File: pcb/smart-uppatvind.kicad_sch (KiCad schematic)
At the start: 65 parts, among them J1 PWR, J2 QWIIC, J3 UART_PROG, J4 FAN, Q1 IRLML9301, Q2 MMBT3904, Q3 MMBT3904, Q4 MMBT3904, Q5 Q_NMOS_GSD, SW1 EN, SW2 MAIN, SW3 BOOT, SW4 FILTER, U1 LDL1117S33R, U2 L7980A, U3 ESP32-C3-WROOM-02, U4 M24C02-WMN

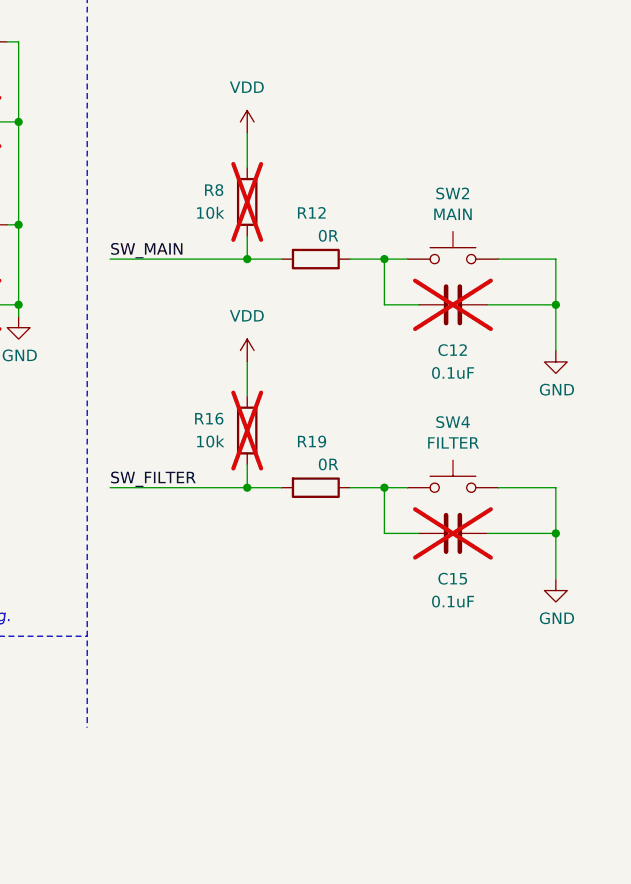
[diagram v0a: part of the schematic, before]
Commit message: Connected shield pins of filter switch, made switch pull-ups not optional
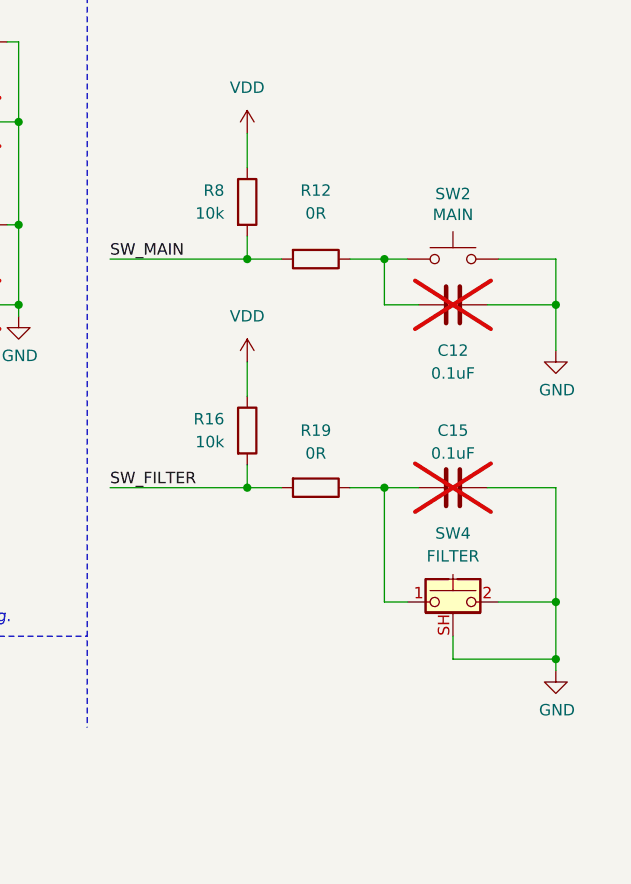
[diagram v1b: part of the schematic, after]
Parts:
- removed SW4: FILTER, Moucha_Primitives:SW_Tactile_G-Switch_GT-TC102B_Angled, symbol Switch:SW_Push
- added SW4: FILTER, Moucha_Primitives:SW_Tactile_G-Switch_GT-TC102B_Angled, symbol Switch:SW_Push_Shielded
- R16, R8: now fitted
- SW2: LCSC C589212 -> (none)
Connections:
- net GND: now also SW4.2, SW4.SH (B)
- net at C15.2, R19.1: now also SW4.1
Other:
- moved on the sheet: C15

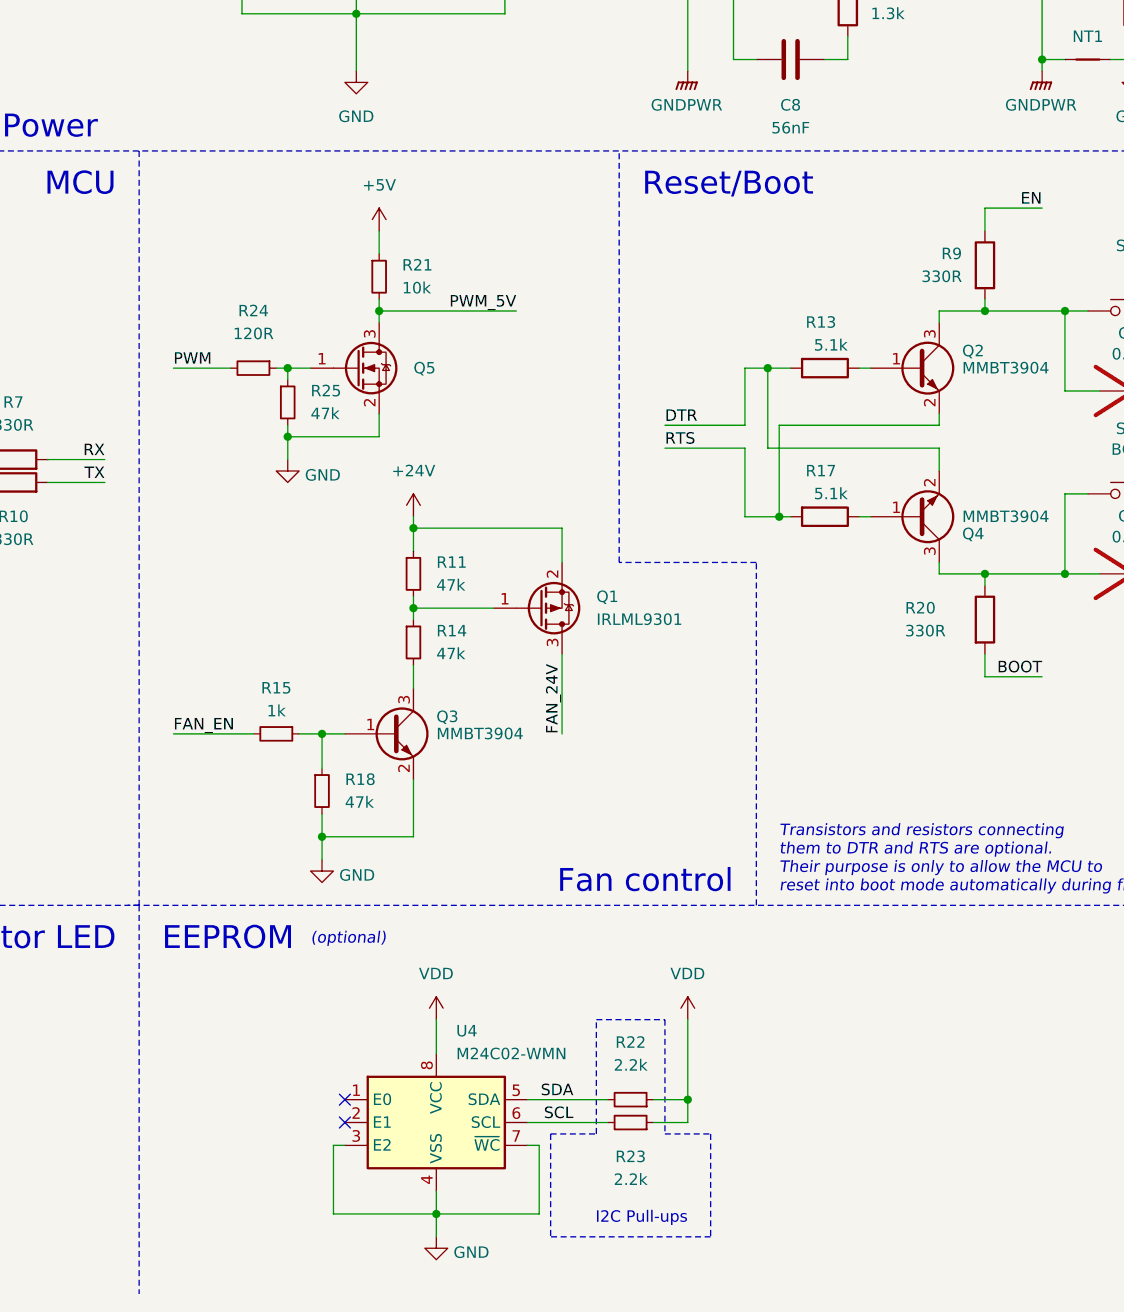
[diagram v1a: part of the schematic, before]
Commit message: Removed R_Small symbols for consistency
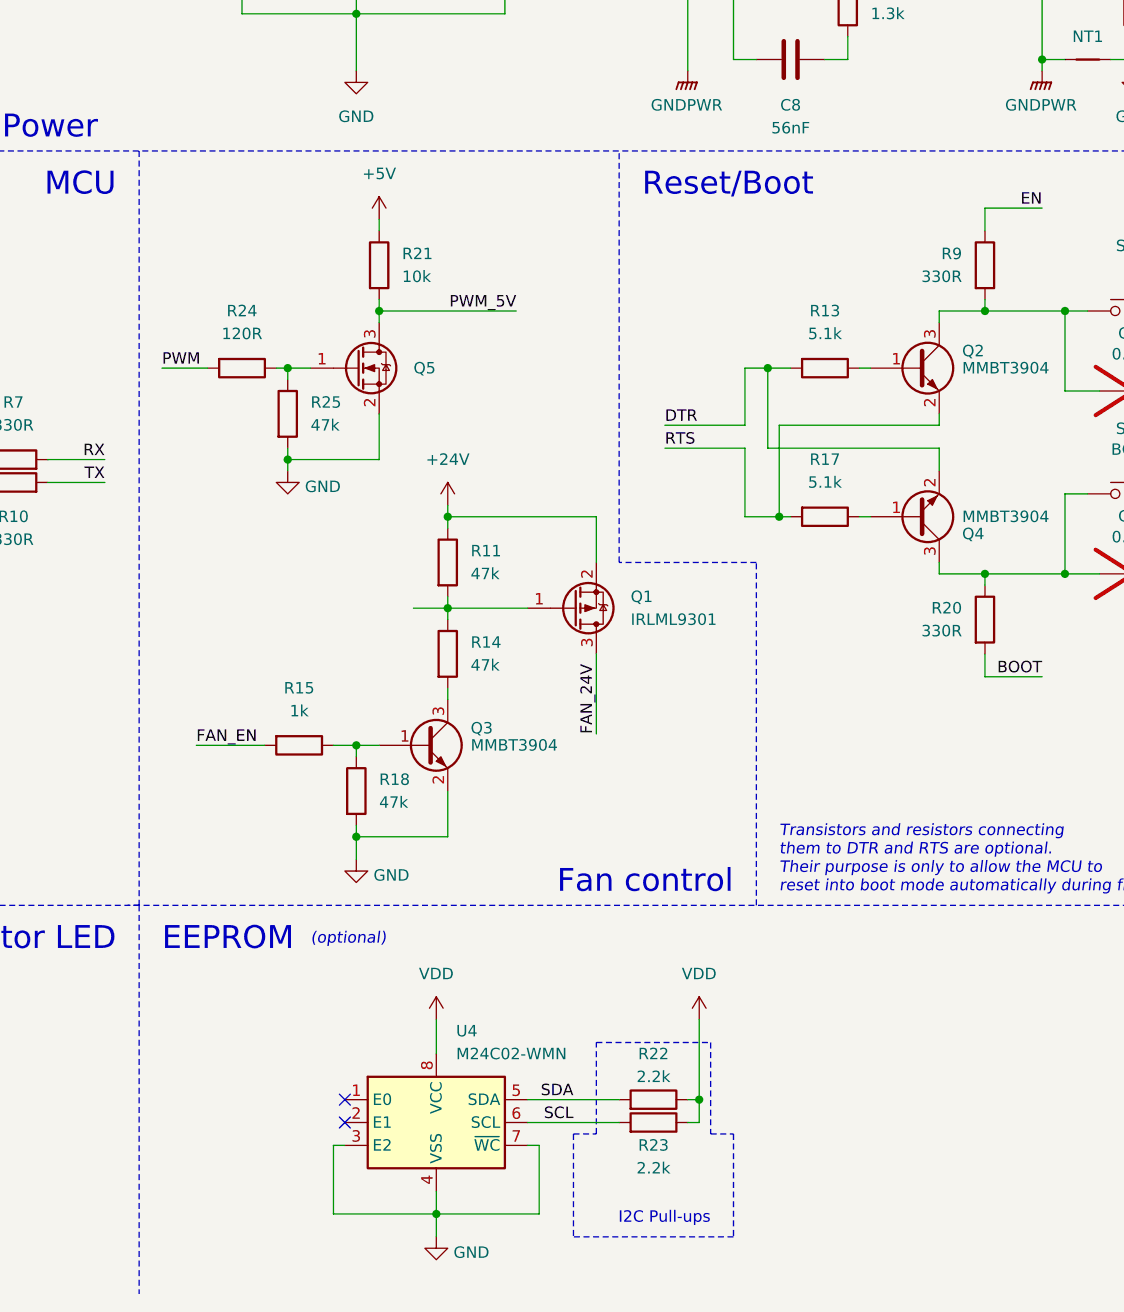
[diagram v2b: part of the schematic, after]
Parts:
- C12, C13, C14, C15: now in the parts list
- R11, R14, R15, R18, R21, R22, R23, R24, R25: symbol Device:R_Small -> Device:R
- R12, R13, R17, R19: LCSC C25905 -> (none)
- R16, R20, R8, R9: LCSC C25104 -> (none)
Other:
- moved on the sheet: Q1, Q3, R11, R14, R15, R18, R21, R22, R23, R24, R25

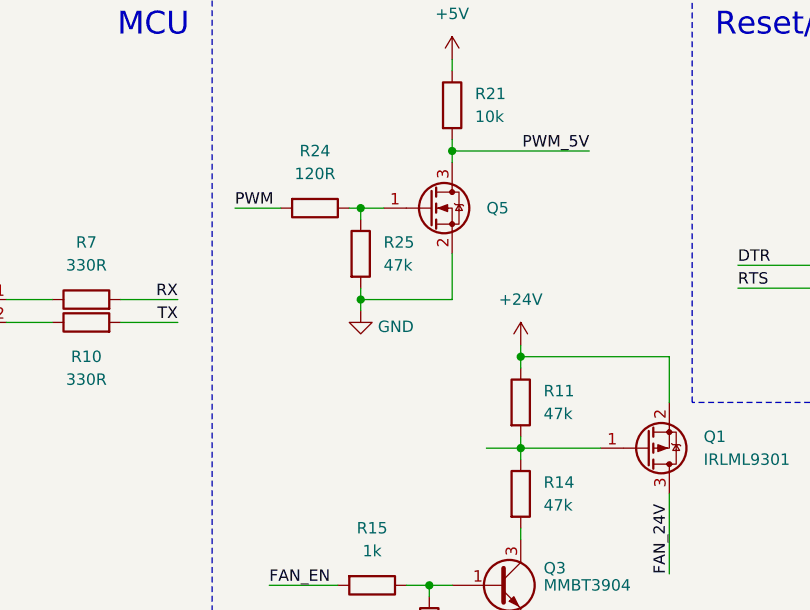
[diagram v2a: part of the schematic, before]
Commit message: Unified resistor footprints - removed handsolder variants
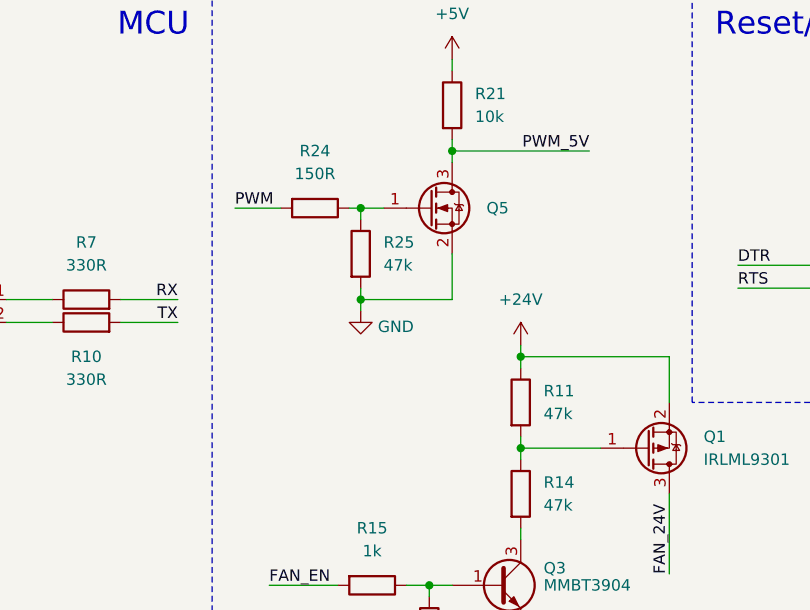
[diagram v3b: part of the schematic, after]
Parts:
- R11, R14, R15, R18, R21, R25: footprint Resistor_SMD:R_0805_2012Metric_Pad1.20x1.40mm_HandSolder -> Resistor_SMD:R_0805_2012Metric
- R24: value 120R -> 150R; footprint Resistor_SMD:R_0805_2012Metric_Pad1.20x1.40mm_HandSolder -> Resistor_SMD:R_0805_2012Metric
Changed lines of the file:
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@@
 	(wire
 		(pts
-			(xy 135.89 121.92) (xy 132.08 121.92)
-		)
-		(stroke
-			(width 0)
-			(type default)
-		)
-	)
-	(wire
-		(pts
 			(xy 154.94 35.56) (xy 167.64 35.56)
 		)
@@
 			)
 		)
-		(property "Footprint" "Resistor_SMD:R_0805_2012Metric_Pad1.20x1.40mm_HandSolder"
+		(property "Footprint" "Resistor_SMD:R_0805_2012Metric"
 			(at 128.27 83.82 0)
 			(effects
@@
 			)
 		)
-		(property "Footprint" "Resistor_SMD:R_0805_2012Metric_Pad1.20x1.40mm_HandSolder"
+		(property "Footprint" "Resistor_SMD:R_0805_2012Metric"
 			(at 134.112 127 90)
 			(effects
@@
 			)
 		)
-		(property "Footprint" "Resistor_SMD:R_0805_2012Metric_Pad1.20x1.40mm_HandSolder"
+		(property "Footprint" "Resistor_SMD:R_0805_2012Metric"
 			(at 119.38 135.382 90)
 			(effects
@@
 			)
 		)
-		(property "Footprint" "Resistor_SMD:R_0805_2012Metric_Pad1.20x1.40mm_HandSolder"
+		(property "Footprint" "Resistor_SMD:R_0805_2012Metric"
 			(at 118.11 100.33 0)
 			(effects
@@
 			)
 		)
-		(property "Footprint" "Resistor_SMD:R_0805_2012Metric_Pad1.20x1.40mm_HandSolder"
+		(property "Footprint" "Resistor_SMD:R_0805_2012Metric"
 			(at 134.112 116.84 90)
 			(effects
@@
 			)
 		)
-		(property "Value" "120R"
+		(property "Value" "150R"
 			(at 113.03 91.44 90)
 			(effects
@@
 			)
 		)
-		(property "Footprint" "Resistor_SMD:R_0805_2012Metric_Pad1.20x1.40mm_HandSolder"
+		(property "Footprint" "Resistor_SMD:R_0805_2012Metric"
 			(at 113.03 95.25 0)
 			(effects
@@
 			)
 		)
-		(property "Footprint" "Resistor_SMD:R_0805_2012Metric_Pad1.20x1.40mm_HandSolder"
+		(property "Footprint" "Resistor_SMD:R_0805_2012Metric"
 			(at 123.952 142.24 90)
 			(effects

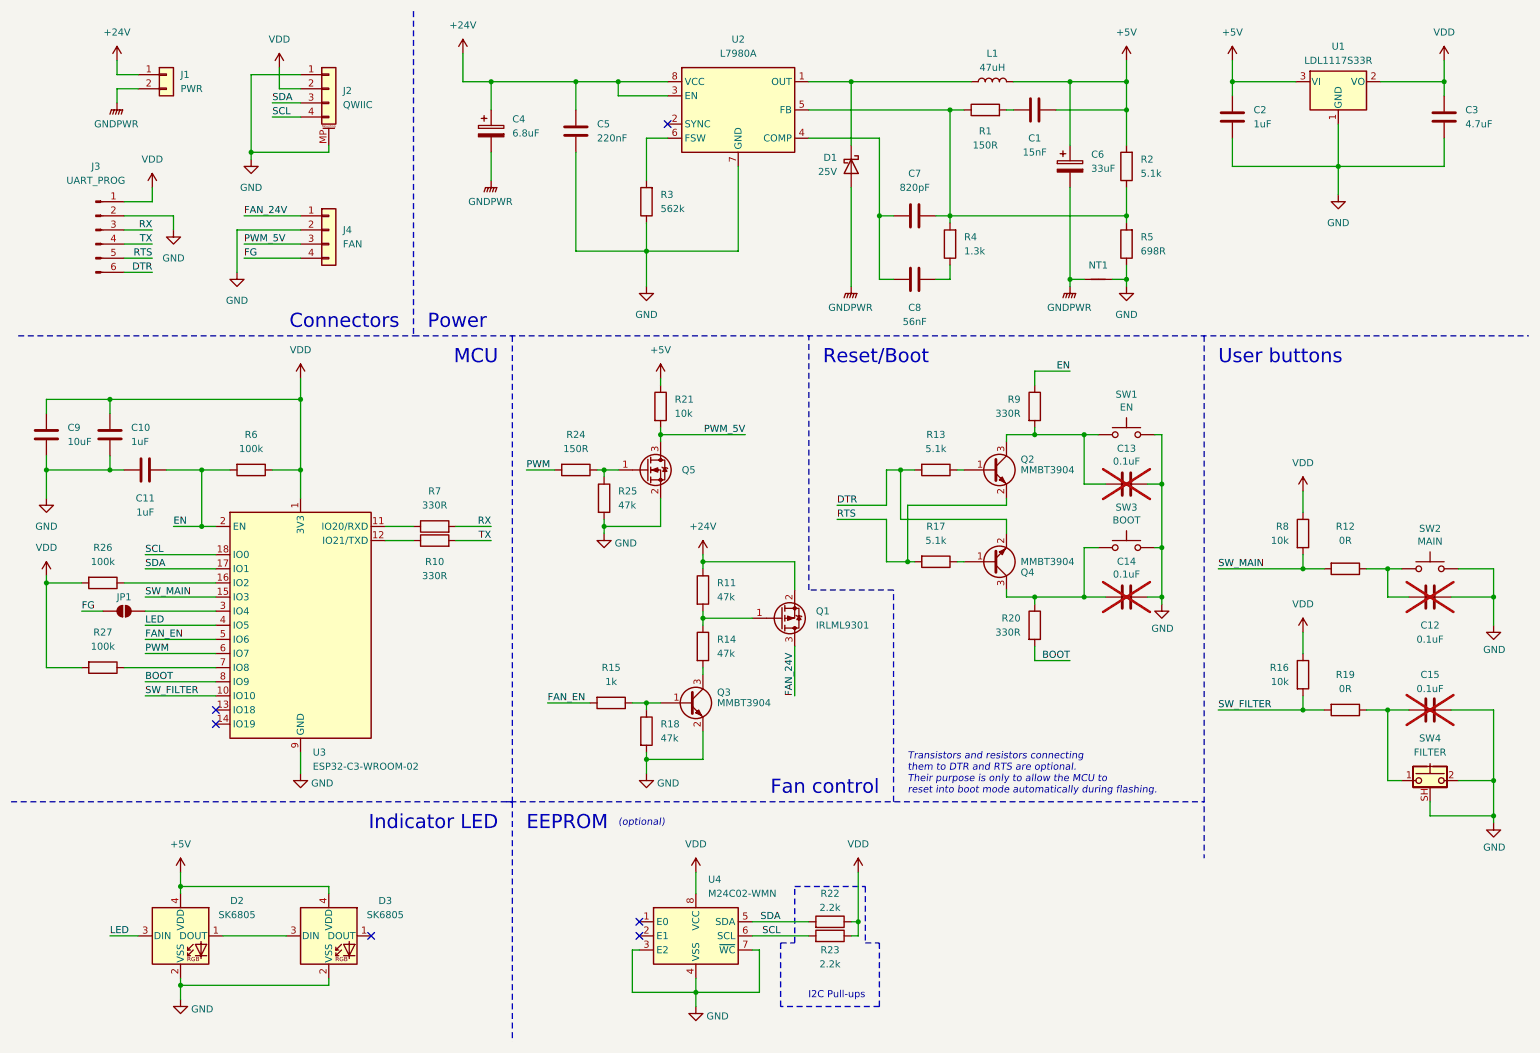
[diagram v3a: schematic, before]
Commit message: Added testpoints
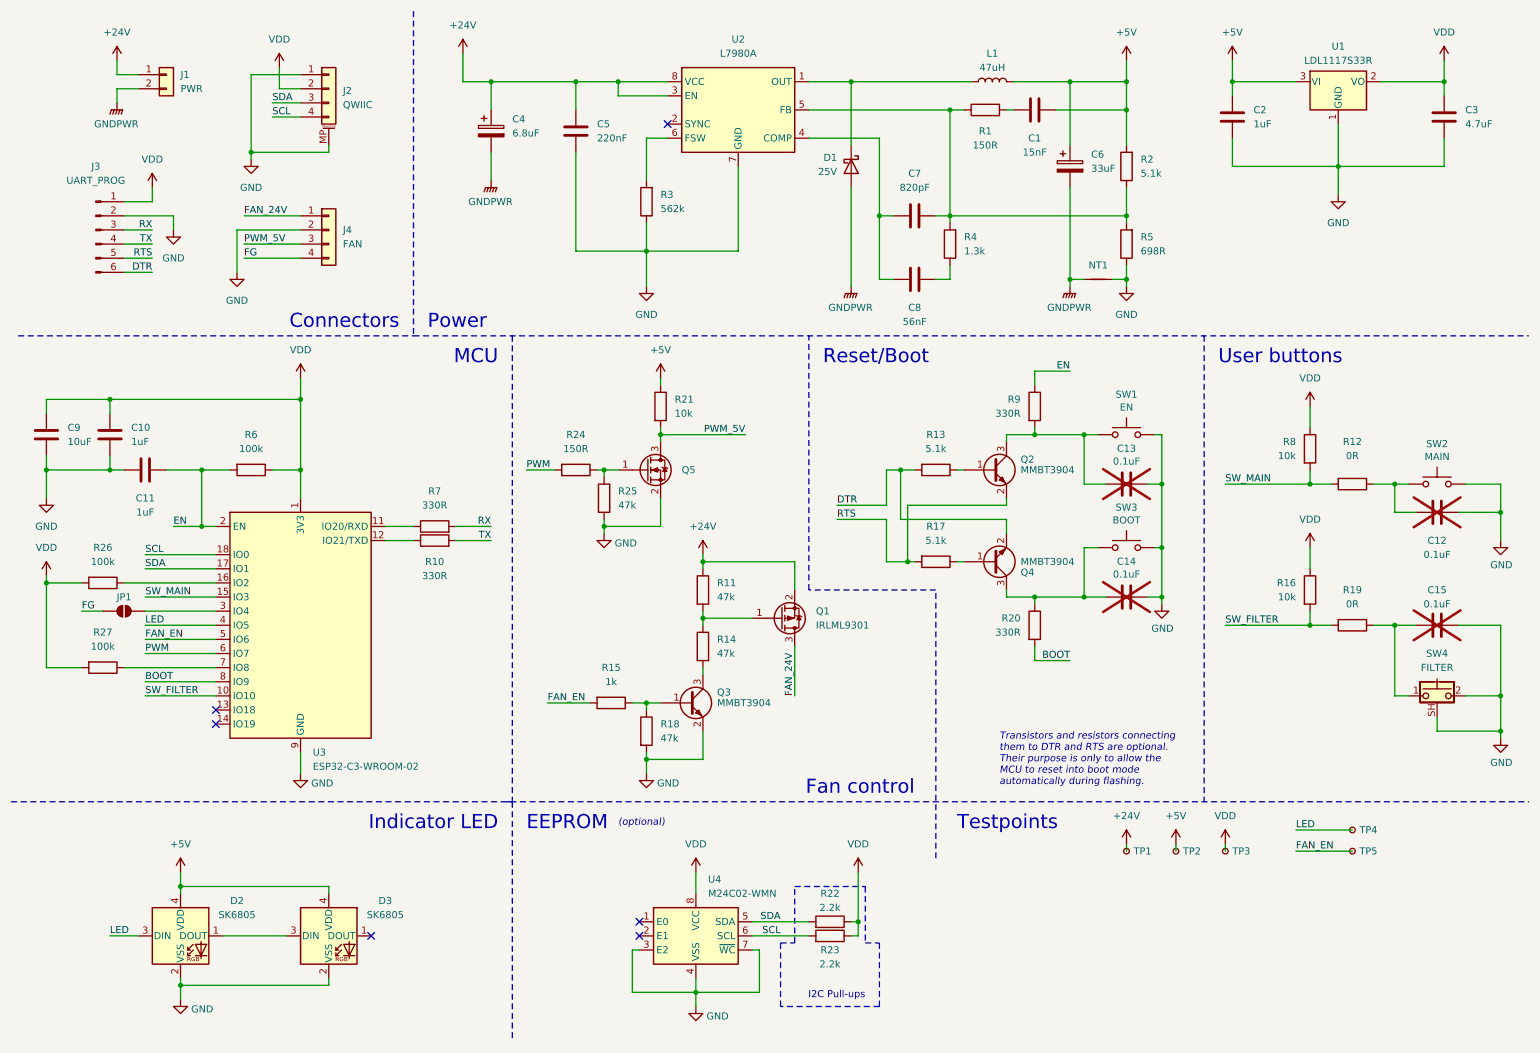
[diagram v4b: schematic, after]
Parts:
- added TP1: VIN, TestPoint:TestPoint_THTPad_1.0x1.0mm_Drill0.5mm, symbol Connector:TestPoint_Small
- added TP2: +5V, TestPoint:TestPoint_THTPad_1.0x1.0mm_Drill0.5mm, symbol Connector:TestPoint_Small
- added TP3: VDD, TestPoint:TestPoint_THTPad_1.0x1.0mm_Drill0.5mm, symbol Connector:TestPoint_Small
- added TP4: LED, TestPoint:TestPoint_Pad_1.0x1.0mm, symbol Connector:TestPoint_Small
- added TP5: FAN_EN, TestPoint:TestPoint_Pad_1.0x1.0mm, symbol Connector:TestPoint_Small
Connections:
- net +24V: now also TP1.1
- net +5V: now also TP2.1
- net FAN_EN: now also TP5.1
- net LED: now also TP4.1
- net VDD: now also TP3.1
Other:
- note added: "Testpoints"
- moved on the sheet: C12, C15, R12, R16, R19, R8, SW2, SW4
